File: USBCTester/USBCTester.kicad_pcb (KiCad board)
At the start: 4 copper layers, 100 x 82.6 mm, 95 parts, among them J1 USB4080-03-A, J2 USB4080-03-A, J3 Conn_01x14, J4 Conn_01x03, J6 Conn_01x03, SW1 SW_Push, U1 74HC595, U2 74HC595, U3 74HC595, U4 74HC595, U5 74HC595, U6 74HC595, U7 RaspberryPi PicoPD

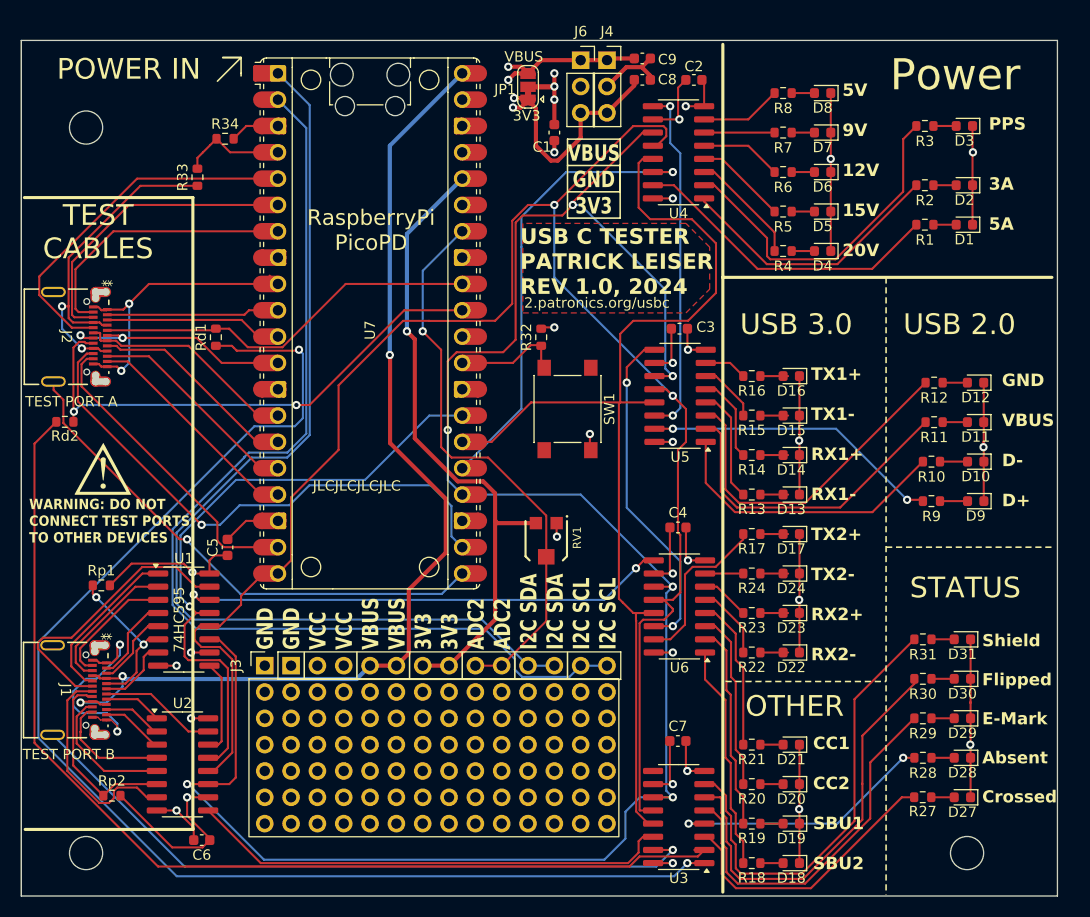
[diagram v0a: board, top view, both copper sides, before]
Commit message: revision 1.2, add another shift register and fix the production files
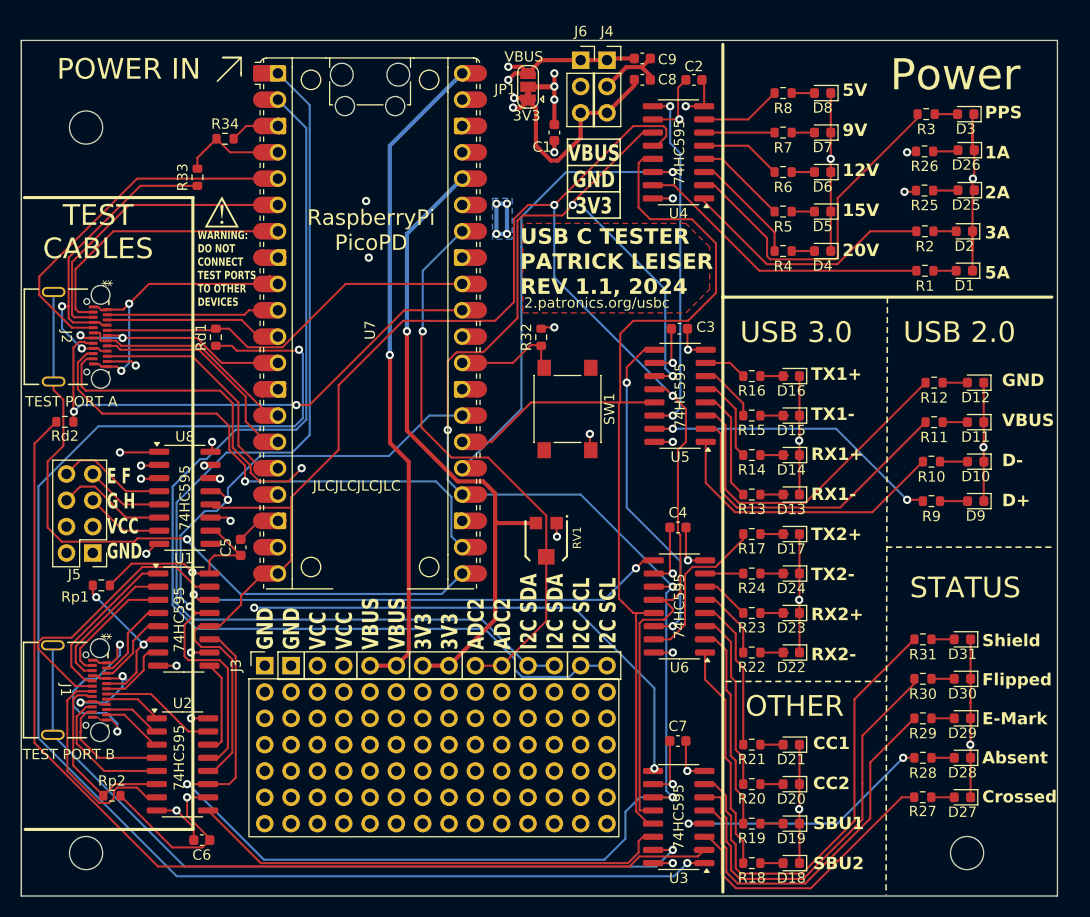
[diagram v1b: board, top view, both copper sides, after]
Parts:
- added D25: LED, LED_SMD:LED_0603_1608Metric, F.Cu at (209.9, 76.0)
- added D26: LED, LED_SMD:LED_0603_1608Metric, F.Cu at (209.9, 72.2)
- added J5: Conn_01x08, Connector_PinHeader_2.54mm:PinHeader_2x04_P2.54mm_Vertical, F.Cu at (125.7, 111.0)
- added R25: R, Resistor_SMD:R_0603_1608Metric, F.Cu at (205.9, 76.1)
- added R26: R, Resistor_SMD:R_0603_1608Metric, F.Cu at (205.9, 72.3)
- added U8: 74HC595, Package_SO:SOIC-16_3.9x9.9mm_P1.27mm, F.Cu at (134.5, 105.7)
- J1, J2: footprint USBCFootprint:USB4080-03-A_GCT_PlatedHoles -> USBCFootprint:USB4080-03-A_GCT_RoundHoles
- U7: value RaspberryPi PicoPD -> RaspberryPi_Pico
- moved D2 4.45 mm to (209.7, 80.0)
- moved R2 4.45 mm to (205.9, 80.0)
- moved D1 4.44 mm to (209.7, 83.8)
- moved R1 4.44 mm to (205.9, 83.8)
- moved C5 1.27 mm to (139.9, 110.5)
- moved D3 1.15 mm to (209.9, 68.7)
- moved R3 1.15 mm to (206.1, 68.7)
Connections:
- J1 pad A1: GND -> Net-(U8-QB)
- J1 pad A12: GND -> Net-(U8-QB)
- J1 pad A4: VBUS -> Net-(U8-QA)
- J1 pad A9: VBUS -> Net-(U8-QA)
- J1 pad B1: GND -> Net-(U8-QB)
- J1 pad B12: GND -> Net-(U8-QB)
- J1 pad B4: VBUS -> Net-(U8-QA)
- J1 pad B9: VBUS -> Net-(U8-QA)
- U3 pad 9: unconnected-(U3-QH'-Pad9) -> Net-(U3-QH')
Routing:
- net Net-(U8-QD): track 0.00 -> 102.5 mm, vias 0 -> 3
- net Net-(U8-QC): track 0.00 -> 95.0 mm, vias 0 -> 3
- net Net-(U3-QH'): track 0.00 -> 63.4 mm, vias 0 -> 3
- net Net-(U8-QB): track 0.00 -> 44.4 mm, vias 0 -> 3
- net VBUS: track 117.6 -> 78.9 mm, vias 5 -> 3
- net Net-(U8-QA): track 0.00 -> 36.3 mm, vias 0 -> 3
- net SRCLK: track 194.2 -> 222.3 mm, vias 6 -> 7
- net Net-(U7-GPIO16): track 50.7 -> 67.7 mm
- net Net-(J5-Pin_6): track 0.00 -> 10.7 mm
- net Net-(J5-Pin_8): track 0.00 -> 10.7 mm
- net Net-(J2-SSTXP2): track 29.9 -> 40.5 mm, vias 0 -> 1
- net Net-(U3-QB): track 129.0 -> 137.9 mm
- net Net-(U3-QA): track 67.2 -> 75.8 mm
- net RCLK: track 171.3 -> 179.2 mm
- net Net-(J5-Pin_7): track 0.00 -> 7.63 mm
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- added copper zone on B.Cu, net GND
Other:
- board text added: "E F G H VCC GND"
- board text added: "PPS 1A 2A 3A 5A"
- board text added: "USB C TESTER PATRICK LEISER REV 1.1, 2024"
- board text removed: "PPS 3A 5A"
- board text removed: "USB C TESTER PATRICK LEISER REV 1.0, 2024"
